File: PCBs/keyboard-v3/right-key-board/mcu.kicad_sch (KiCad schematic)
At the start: 11 parts, among them J301 F31Z1A7H111008, U301 STM32U031C6Ux

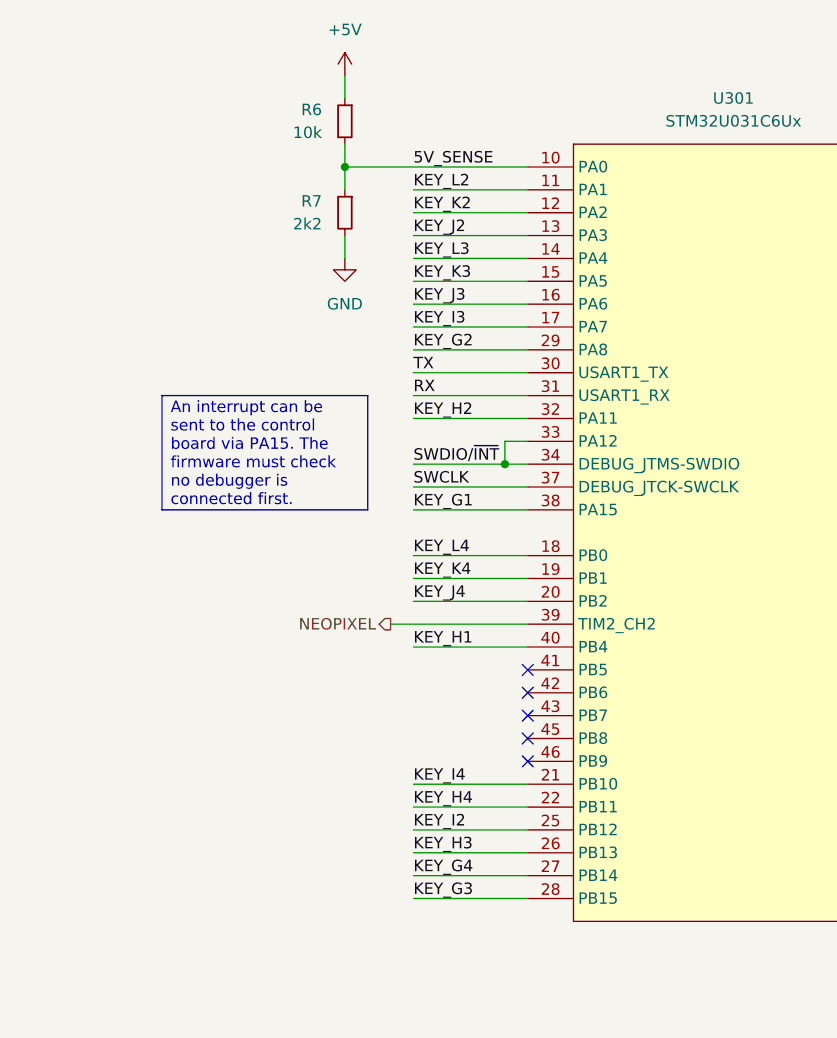
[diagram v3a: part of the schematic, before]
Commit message: Left key board done
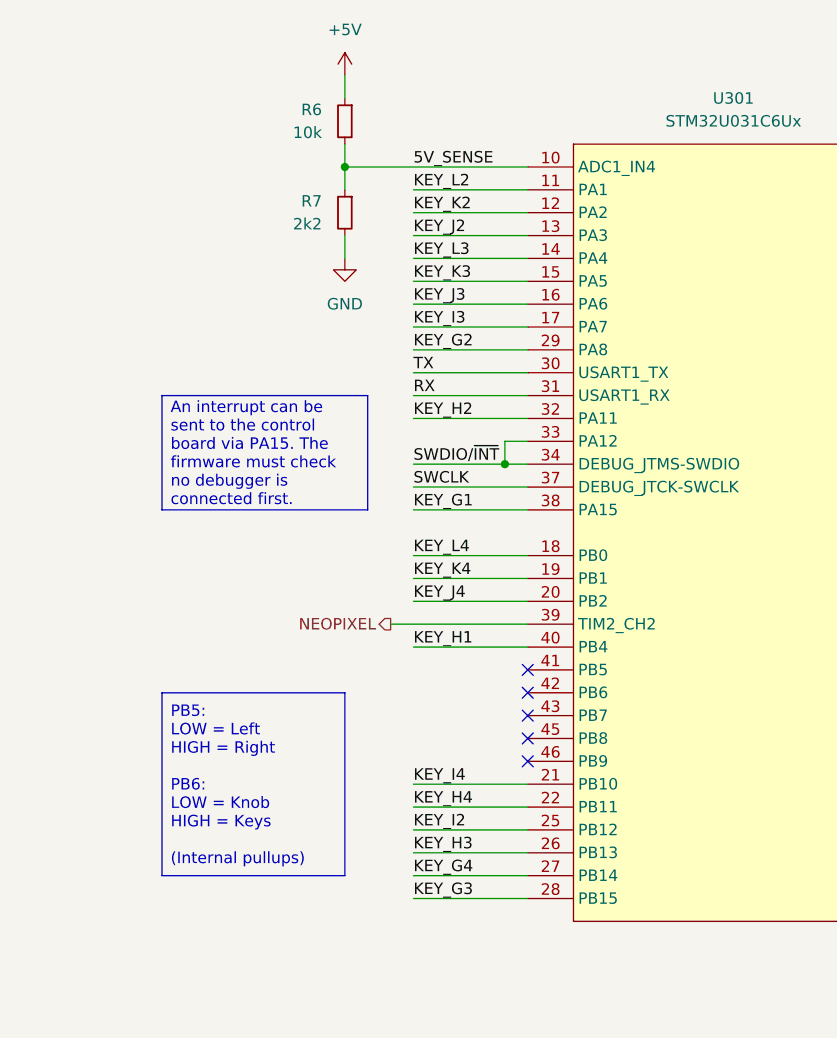
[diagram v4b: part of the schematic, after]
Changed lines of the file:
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@@
+		)
+	)
+	(text_box "PB5:\nLOW = Left\nHIGH = Right\n\nPB6:\nLOW = Knob\nHIGH = Keys\n\n(Internal pullups)"
+		(exclude_from_sim no)
+		(at 58.42 111.76 0)
+		(size 20.32 20.32)
+		(margins 0.9525 0.9525 0.9525 0.9525)
+		(stroke
+			(width 0)
+			(type solid)
+		)
+		(fill
+			(type none)
+		)
+		(effects
+			(font
+				(size 1.27 1.27)
+			)
+			(justify left)
 		)
 	)
@@
 	)
 	(no_connect
+		(at 99.06 111.76)
+	)
+	(no_connect
 		(at 99.06 119.38)
 	)
 	(no_connect
 		(at 99.06 114.3)
-	)
-	(no_connect
-		(at 99.06 111.76)
 	)
 	(no_connect
@@
 		)
 		(pin "10"
+			(alternate "ADC1_IN4")
 		)
 		(pin "41"
